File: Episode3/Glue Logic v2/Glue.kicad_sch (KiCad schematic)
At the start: 8 parts, among them U7 ATF22V10C, U8 ATF750CL, U9 ATF750CL

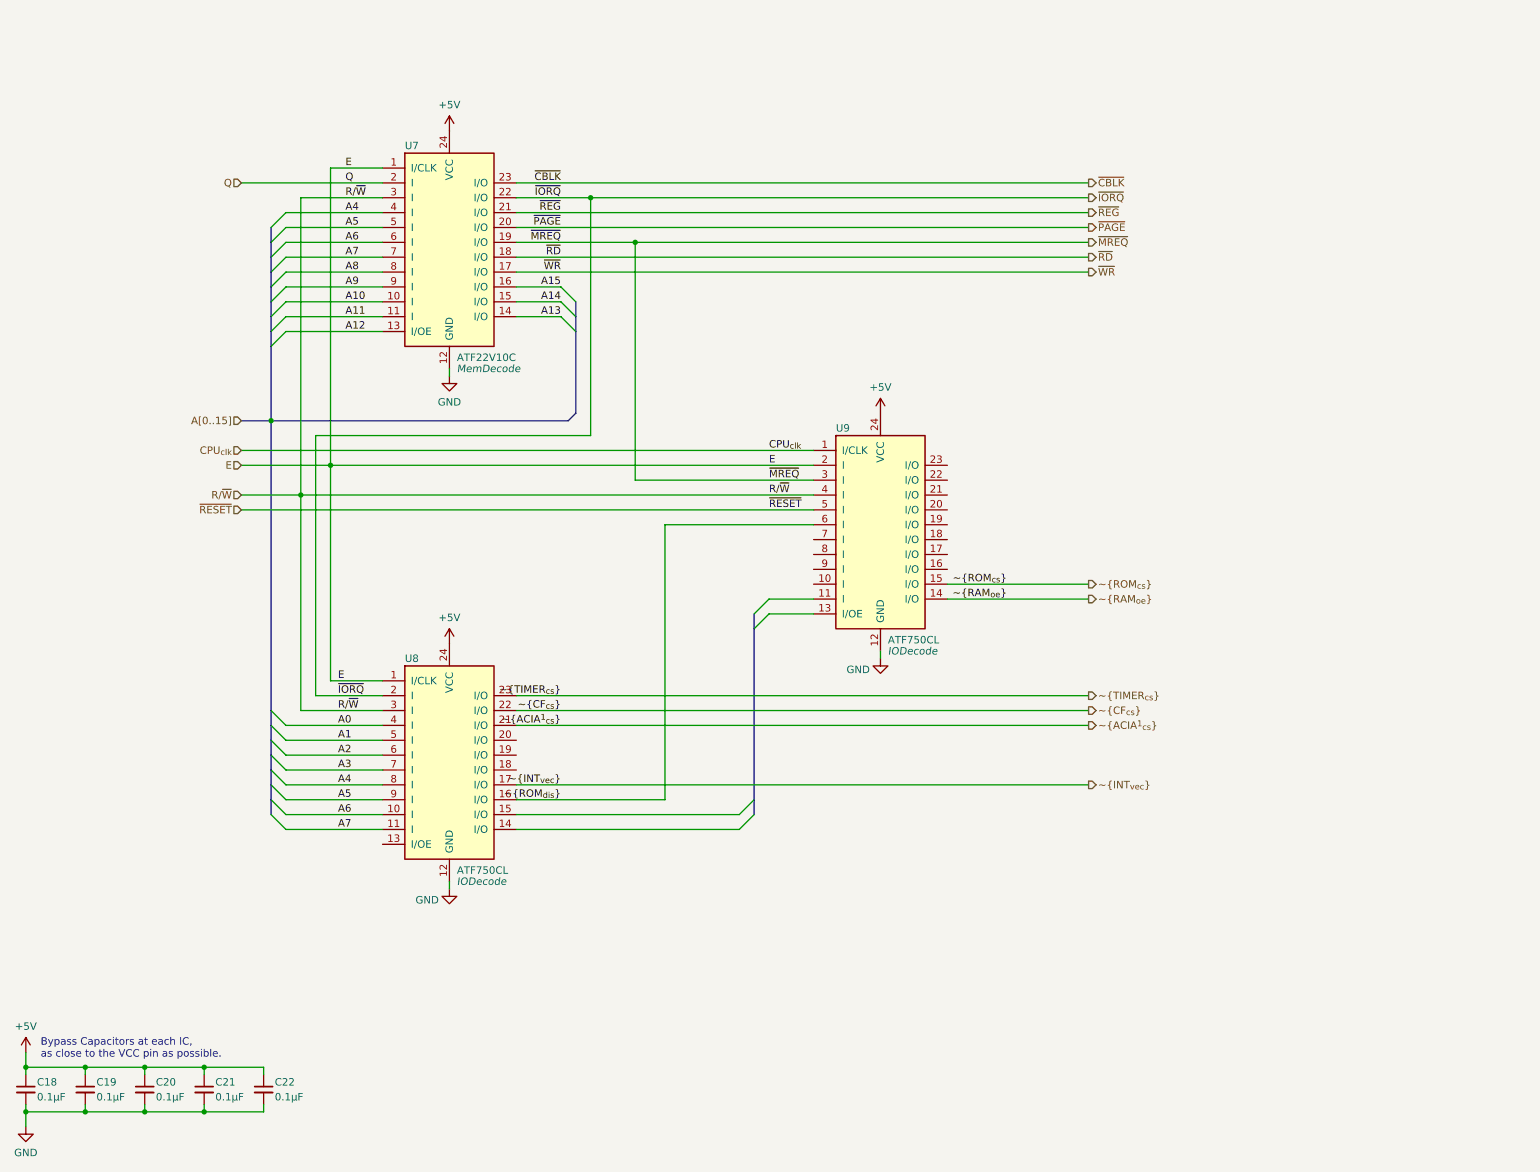
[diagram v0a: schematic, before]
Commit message: changed strategy and simplified things
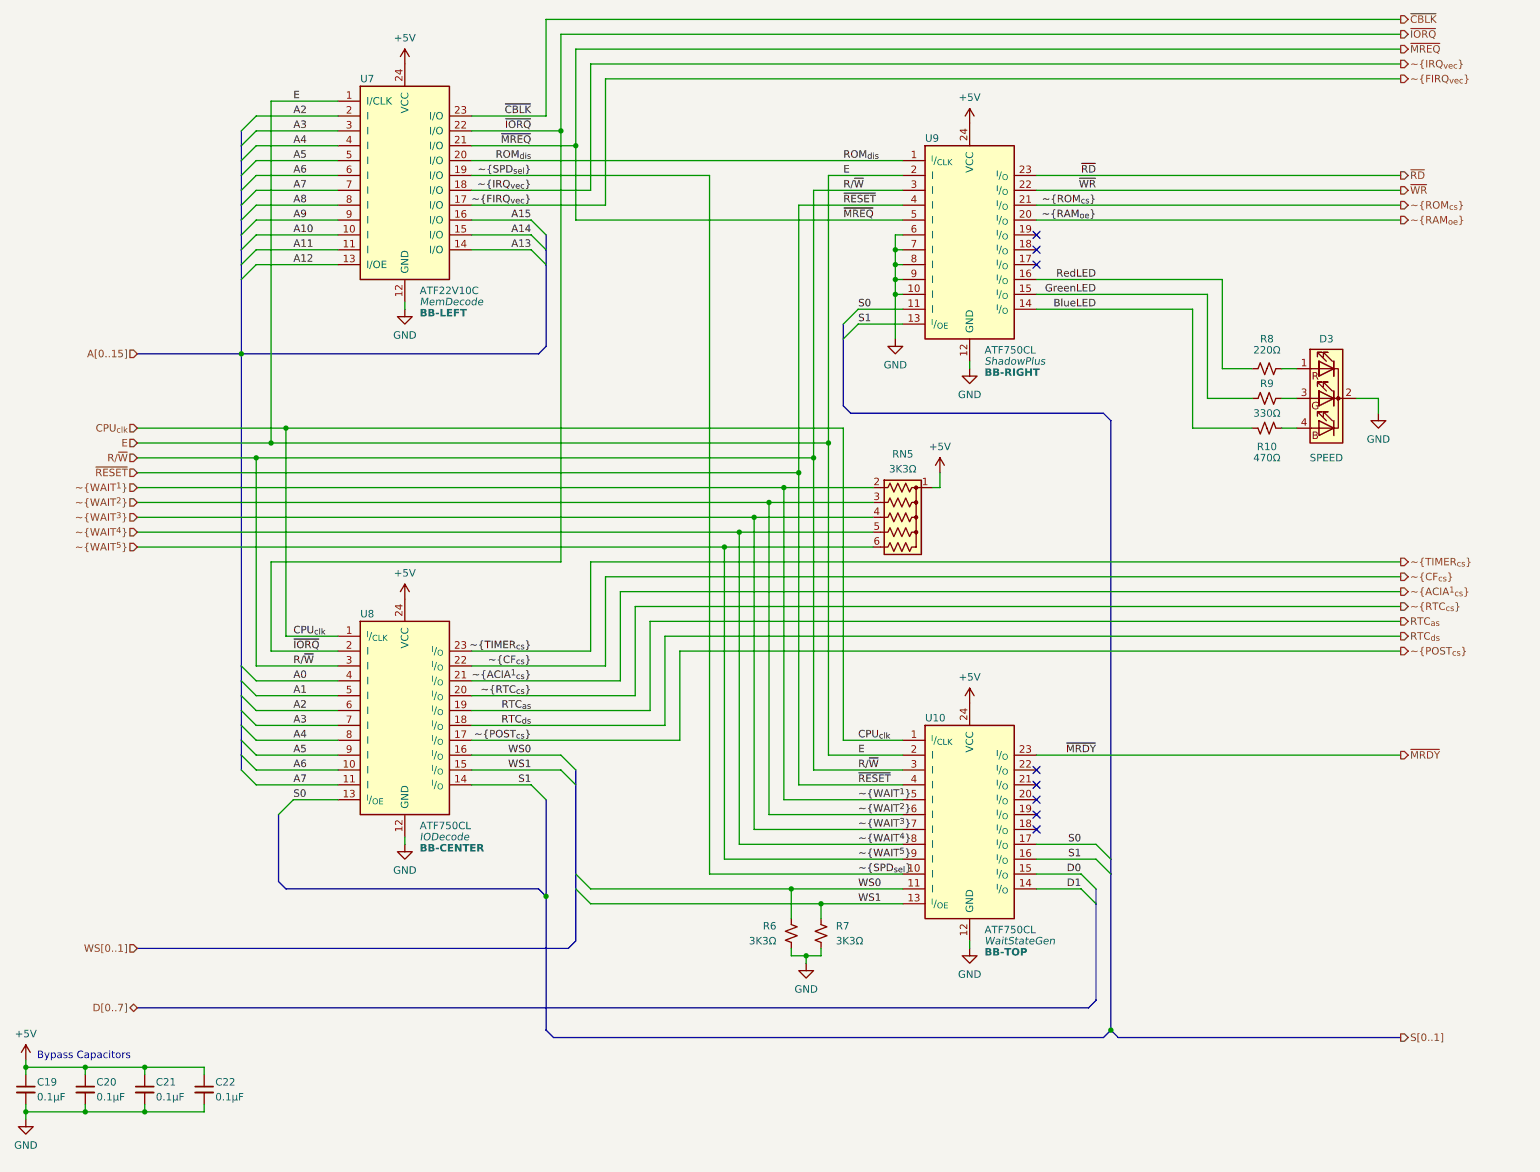
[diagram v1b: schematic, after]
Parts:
- removed C22: 0.1µF, symbol Device:C_Small
- added D3: SPEED, symbol Device:LED_RKGB
- added R10: 470Ω, symbol Device:R_Small_US
- added R6, R7: 3K3Ω, symbol Device:R_Small_US
- added R8: 220Ω, symbol Device:R_Small_US
- added R9: 330Ω, symbol Device:R_Small_US
- added RN5: 3K3Ω, Resistor_THT:R_Array_SIP6, symbol Device:R_Network05_US
- added U9: ATF750CL, Package_DIP:DIP-24_W7.62mm_Socket_LongPads, symbol MicroHobbyist:ATF750C
- U10: renamed from U9; symbol MicroHobbyist:ATF22V10C -> MicroHobbyist:ATF750C; File IODecode -> WaitStateGen; Position BB-Center -> BB-TOP
- U7: Position BB-Left -> BB-LEFT
- U8: symbol MicroHobbyist:ATF22V10C -> MicroHobbyist:ATF750C; Position BB-Center -> BB-CENTER
- renumbered C18 to C19, C19 to C20, C20 to C21, C21 to C22
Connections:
- net Q is gone; now on net A2: U7.2 (I)
- net ~{REG} is gone; now on net ~{MREQ}: U7.21 (I/O)
- net +5V: now also RN5.1 (common), U9.24 (VCC)
- net A3: now also U7.3 (I)
- net CPU_{clk}: now also U8.1 (^{I}/_{CLK})
- net E: now also U9.2 (I); no longer U8.1 (I/CLK)
- net GND: now also D3.2 (K), R6.1, R7.1, U9.10 (I), U9.12 (GND), U9.6 (I), U9.7 (I), U9.8 (I), U9.9 (I)
- net R/~{W}: now also U10.3 (I), U9.3 (I); no longer U10.4 (I), U7.3 (I)
- net ~{MREQ}: now also U9.5 (I); no longer U10.3 (I), U7.19 (I/O)
- net ~{RAM_{oe}}: now also U9.20 (^{I}/_{O}); no longer U10.14 (I/O)
- net ~{RD}: now also U9.23 (^{I}/_{O}); no longer U7.18 (I/O)
- net ~{RESET}: now also U10.4 (I), U9.4 (I); no longer U10.5 (I)
- net ~{ROM_{cs}}: now also U9.21 (^{I}/_{O}); no longer U10.15 (I/O)
- net ~{WR}: now also U9.22 (^{I}/_{O}); no longer U7.17 (I/O)
- net S0: now reaches U8.13 (^{I}/_{OE})
- net S0: now also U10.17 (^{I}/_{O}), U9.11 (I)
- net S1: now reaches U8.14 (^{I}/_{O})
- net S1: now also U10.16 (^{I}/_{O}), U9.13 (^{I}/_{OE})
- net WS1: now reaches U8.15 (^{I}/_{O})
- net WS1: now also U10.13 (^{I}/_{OE}), R7.2
- net RTC_{ds}: now reaches U8.18 (^{I}/_{O})
- net RTC_{as}: now reaches U8.19 (^{I}/_{O})
- net ~{RTC_{cs}}: now reaches U8.20 (^{I}/_{O})
- net ~{SPD_{sel}}: now reaches U10.10 (I)
- net ~{SPD_{sel}}: now also U7.19 (I/O)
- net WS0: now reaches U10.11 (I)
- net WS0: now also U8.16 (^{I}/_{O}), R6.2
- net ~{MRDY}: now reaches U10.23 (^{I}/_{O})
- net ~{WAIT^{3}}: now reaches U10.7 (I)
- net ~{WAIT^{3}}: now also RN5.4 (R3)
- net ~{WAIT^{4}}: now reaches U10.8 (I)
- net ~{WAIT^{4}}: now also RN5.5 (R4)
- net ~{WAIT^{5}}: now reaches U10.9 (I)
- net ~{WAIT^{5}}: now also RN5.6 (R5)
- net ~{INT_{vec}} renamed ~{POST_{cs}}
- net ~{PAGE} renamed ROM_{dis}
- net ROM_{dis}: now also U9.1 (^{I}/_{CLK})
- net ~{ROM_{dis}} renamed ~{WAIT^{2}}
- net ~{WAIT^{2}}: now also RN5.3 (R2); no longer U8.16 (I/O)
- new net: D3.1 (RA), R8.2
- new net: D3.3 (GA), R9.2
- new net: D3.4 (BA), R10.2
- new net BlueLED: R10.1, U9.14 (^{I}/_{O})
- new net D0: U10.15 (^{I}/_{O})
- new net D1: U10.14 (^{I}/_{O})
- new net GreenLED: R9.1, U9.15 (^{I}/_{O})
- new net RedLED: R8.1, U9.16 (^{I}/_{O})
- new net ~{FIRQ_{vec}}: U7.17 (I/O)
- new net ~{IRQ_{vec}}: U7.18 (I/O)
- new net ~{WAIT^{1}}: RN5.2 (R1), U10.5 (I)
- no-connect marks 0 -> 8
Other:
- note added: "Bypass Capacitors"
- note removed: "Bypass Capacitors at each IC, as close to the VCC pin as possible."
- moved on the sheet: U10, U7, U8

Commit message: Massive changes to the PLD code (tested) - Minor changes to the Schematic
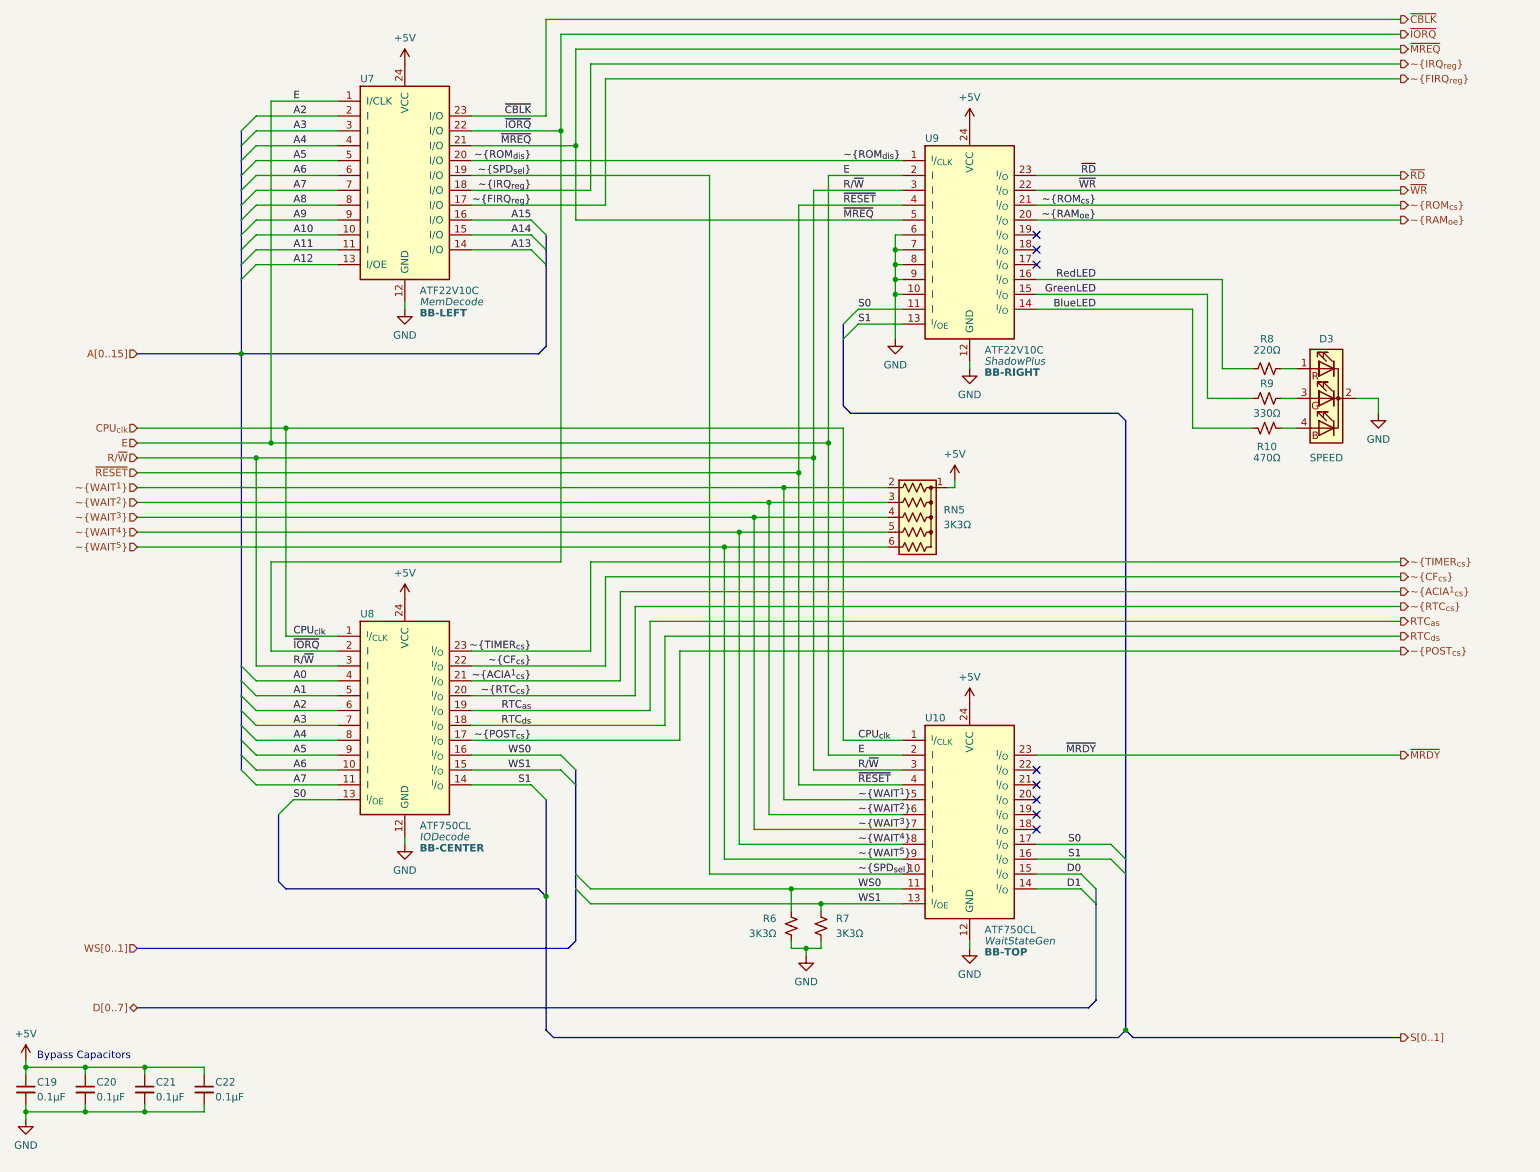
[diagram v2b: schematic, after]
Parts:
- U9: value ATF750CL -> ATF22V10C
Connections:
- net ROM_{dis} renamed ~{ROM_{dis}}
- net ~{FIRQ_{vec}} renamed ~{FIRQ_{reg}}
- net ~{IRQ_{vec}} renamed ~{IRQ_{reg}}
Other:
- title: Programmable Logic Devices -> Glue Logic with PLDs
- moved on the sheet: R6, R7, RN5
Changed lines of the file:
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@@
 	(paper "USLetter")
 	(title_block
-		(title "Programmable Logic Devices")
-		(date "2025-12-06")
+		(title "Glue Logic with PLDs")
+		(date "2026-02-07")
 		(rev "2.0")
 		(company "MicroHobbyist")
@@
 	)
 	(junction
-		(at 198.12 185.42)
+		(at 200.66 185.42)
 		(diameter 0)
 		(color 0 0 0 0)
@@
 	)
 	(junction
-		(at 146.05 172.72)
+		(at 146.05 171.45)
 		(diameter 0)
 		(color 0 0 0 0)
@@
 	)
 	(bus_entry
-		(at 195.58 156.21)
+		(at 198.12 156.21)
 		(size 2.54 2.54)
 		(stroke
@@
 	)
 	(bus_entry
-		(at 195.58 153.67)
+		(at 198.12 153.67)
 		(size 2.54 2.54)
 		(stroke
@@
 	(wire
 		(pts
-			(xy 139.7 95.25) (xy 157.48 95.25)
+			(xy 139.7 95.25) (xy 160.02 95.25)
 		)
 		(stroke
@@
 	(wire
 		(pts
-			(xy 143.51 171.45) (xy 143.51 172.72)
+			(xy 143.51 170.18) (xy 143.51 171.45)
 		)
 		(stroke
@@
 	(bus
 		(pts
-			(xy 199.39 186.69) (xy 247.65 186.69)
+			(xy 201.93 186.69) (xy 247.65 186.69)
 		)
 		(stroke
@@
 	(wire
 		(pts
-			(xy 167.64 92.71) (xy 168.91 92.71)
+			(xy 170.18 92.71) (xy 171.45 92.71)
 		)
 		(stroke
@@
 	(wire
 		(pts
-			(xy 146.05 172.72) (xy 148.59 172.72)
+			(xy 146.05 171.45) (xy 148.59 171.45)
 		)
 		(stroke
@@
 	(wire
 		(pts
-			(xy 132.08 102.87) (xy 157.48 102.87)
+			(xy 132.08 102.87) (xy 160.02 102.87)
 		)
 		(stroke
@@
 	(bus
 		(pts
-			(xy 198.12 156.21) (xy 198.12 158.75)
+			(xy 200.66 156.21) (xy 200.66 158.75)
 		)
 		(stroke
@@
 	(bus
 		(pts
-			(xy 198.12 81.28) (xy 196.85 80.01)
+			(xy 200.66 81.28) (xy 199.39 80.01)
 		)
 		(stroke
@@
 	(wire
 		(pts
-			(xy 185.42 156.21) (xy 195.58 156.21)
+			(xy 185.42 156.21) (xy 198.12 156.21)
 		)
 		(stroke
@@
 	(bus
 		(pts
-			(xy 198.12 185.42) (xy 199.39 186.69)
+			(xy 200.66 185.42) (xy 201.93 186.69)
 		)
 		(stroke
@@
 	(wire
 		(pts
-			(xy 168.91 90.17) (xy 168.91 92.71)
+			(xy 171.45 91.44) (xy 171.45 92.71)
 		)
 		(stroke
@@
 	(wire
 		(pts
-			(xy 148.59 163.83) (xy 148.59 166.37)
+			(xy 148.59 163.83) (xy 148.59 165.1)
 		)
 		(stroke
@@
 	(bus
 		(pts
-			(xy 198.12 185.42) (xy 196.85 186.69)
+			(xy 200.66 185.42) (xy 199.39 186.69)
 		)
 		(stroke
@@
 	(bus
 		(pts
-			(xy 102.87 186.69) (xy 196.85 186.69)
+			(xy 102.87 186.69) (xy 199.39 186.69)
 		)
 		(stroke
@@
 	(wire
 		(pts
-			(xy 142.24 92.71) (xy 157.48 92.71)
+			(xy 142.24 92.71) (xy 160.02 92.71)
 		)
 		(stroke
@@
 	(wire
 		(pts
-			(xy 134.62 100.33) (xy 157.48 100.33)
+			(xy 134.62 100.33) (xy 160.02 100.33)
 		)
 		(stroke
@@
 	(bus
 		(pts
-			(xy 196.85 80.01) (xy 153.67 80.01)
+			(xy 199.39 80.01) (xy 153.67 80.01)
 		)
 		(stroke
@@
 	(wire
 		(pts
-			(xy 185.42 153.67) (xy 195.58 153.67)
+			(xy 185.42 153.67) (xy 198.12 153.67)
 		)
 		(stroke
@@
 	(wire
 		(pts
-			(xy 148.59 171.45) (xy 148.59 172.72)
+			(xy 148.59 170.18) (xy 148.59 171.45)
 		)
 		(stroke
@@
 	(bus
 		(pts
-			(xy 198.12 158.75) (xy 198.12 185.42)
+			(xy 200.66 158.75) (xy 200.66 185.42)
 		)
 		(stroke
@@
 	(wire
 		(pts
-			(xy 143.51 172.72) (xy 146.05 172.72)
+			(xy 143.51 171.45) (xy 146.05 171.45)
 		)
 		(stroke
@@
 	(wire
 		(pts
-			(xy 137.16 97.79) (xy 157.48 97.79)
+			(xy 137.16 97.79) (xy 160.02 97.79)
 		)
 		(stroke
@@
 	(bus
 		(pts
-			(xy 198.12 156.21) (xy 198.12 81.28)
+			(xy 200.66 156.21) (xy 200.66 81.28)
 		)
 		(stroke
@@
 	(wire
 		(pts
-			(xy 146.05 172.72) (xy 146.05 173.99)
+			(xy 146.05 171.45) (xy 146.05 172.72)
 		)
 		(stroke
@@
 	(wire
 		(pts
-			(xy 143.51 161.29) (xy 143.51 166.37)
+			(xy 143.51 161.29) (xy 143.51 165.1)
 		)
 		(stroke
@@
 		)
 	)
-	(label "ROM_{dis}"
+	(label "~{ROM_{dis}}"
 		(at 152.4 36.83 0)
 		(effects
@@
 		)
 	)
-	(label "~{FIRQ_{vec}}"
+	(label "~{FIRQ_{reg}}"
 		(at 99.06 44.45 180)
 		(effects
@@
 		)
 	)
-	(label "ROM_{dis}"
+	(label "~{ROM_{dis}}"
 		(at 99.06 36.83 180)
 		(effects
@@
 		)
 	)
-	(label "~{IRQ_{vec}}"
+	(label "~{IRQ_{reg}}"
 		(at 99.06 41.91 180)
 		(effects
@@
 		)
 	)
-	(hierarchical_label "~{IRQ_{vec}}"
+	(hierarchical_label "~{IRQ_{reg}}"
 		(shape output)
 		(at 247.65 20.32 0)
@@
 		)
 	)
-	(hierarchical_label "~{FIRQ_{vec}}"
+	(hierarchical_label "~{FIRQ_{reg}}"
 		(shape output)
 		(at 247.65 22.86 0)
@@
 	(symbol
 		(lib_id "power:+5V")
-		(at 168.91 90.17 0)
+		(at 171.45 91.44 0)
 		(unit 1)
 		(exclude_from_sim no)
@@
 		(dnp no)
 		(property "Reference" "#PWR042"
-			(at 168.91 93.98 0)
+			(at 171.45 95.25 0)
 			(effects
 				(font
@@
 		)
 		(property "Value" "+5V"
-			(at 168.91 85.725 0)
+			(at 171.45 86.995 0)
 			(effects
 				(font
@@
 		)
 		(property "Footprint" ""
-			(at 168.91 90.17 0)
+			(at 171.45 91.44 0)
 			(effects
 				(font
@@
 		)
 		(property "Datasheet" ""
-			(at 168.91 90.17 0)
+			(at 171.45 91.44 0)
 			(effects
 				(font
@@
 		)
 		(property "Description" "Power symbol creates a global label with name \"+5V\""
-			(at 168.91 90.17 0)
+			(at 171.45 91.44 0)
 			(effects
 				(font
@@
 	(symbol
 		(lib_id "Device:R_Network05_US")
-		(at 162.56 97.79 270)
+		(at 165.1 97.79 270)
 		(unit 1)
 		(exclude_from_sim no)
@@
 		(dnp no)
 		(property "Reference" "RN5"
-			(at 162.56 86.995 90)
+			(at 169.545 96.52 90)
 			(effects
 				(font
 					(size 1.27 1.27)
 				)
+				(justify left)
 			)
 		)
 		(property "Value" "3K3Ω"
-			(at 162.56 89.535 90)
+			(at 169.545 99.06 90)
 			(effects
 				(font
 					(size 1.27 1.27)
 				)
+				(justify left)
 			)
 		)
 		(property "Footprint" "Resistor_THT:R_Array_SIP6"
-			(at 162.56 107.315 90)
+			(at 165.1 107.315 90)
 			(effects
 				(font
@@
 		)
 		(property "Datasheet" "http://www.vishay.com/docs/31509/csc.pdf"
-			(at 162.56 97.79 0)
+			(at 165.1 97.79 0)
 			(effects
 				(font
@@
 		)
 		(property "Description" "5 resistor network, star topology, bussed resistors, small US symbol"
-			(at 162.56 97.79 0)
+			(at 165.1 97.79 0)
 			(effects
 				(font
@@
 		(lib_name "GND_1")
 		(lib_id "power:GND")
-		(at 146.05 173.99 0)
+		(at 146.05 172.72 0)
 		(unit 1)
 		(exclude_from_sim no)
@@
 		(dnp no)
 		(property "Reference" "#PWR040"
-			(at 146.05 180.34 0)
+			(at 146.05 179.07 0)
 			(effects
 				(font
@@
 		)
 		(property "Value" "GND"
-			(at 146.05 178.435 0)
+			(at 146.05 177.165 0)
 			(effects
 				(font
@@
 		)
 		(property "Footprint" ""
-			(at 146.05 173.99 0)
+			(at 146.05 172.72 0)
 			(effects
 				(font
@@
 		)
 		(property "Datasheet" ""
-			(at 146.05 173.99 0)
+			(at 146.05 172.72 0)
 			(effects
 				(font
@@
 		)
 		(property "Description" "Power symbol creates a global label with name \"GND\" , ground"
-			(at 146.05 173.99 0)
+			(at 146.05 172.72 0)
 			(effects
 				(font
@@
 	(symbol
 		(lib_id "Device:R_Small_US")
-		(at 148.59 168.91 180)
+		(at 148.59 167.64 180)
 		(unit 1)
 		(exclude_from_sim no)
@@
 		(fields_autoplaced yes)
 		(property "Reference" "R7"
-			(at 151.13 167.6399 0)
+			(at 151.13 166.3699 0)
 			(effects
 				(font
@@
 		)
 		(property "Value" "3K3Ω"
-			(at 151.13 170.1799 0)
+			(at 151.13 168.9099 0)
 			(effects
 				(font
@@
 		)
 		(property "Footprint" ""
-			(at 148.59 168.91 0)
+			(at 148.59 167.64 0)
 			(effects
 				(font
@@
 		)
 		(property "Datasheet" "~"
-			(at 148.59 168.91 0)
+			(at 148.59 167.64 0)
 			(effects
 				(font
@@
 		)
 		(property "Description" "Resistor, small US symbol"
-			(at 148.59 168.91 0)
+			(at 148.59 167.64 0)
 			(effects
 				(font
@@
 			)
 		)
-		(property "Value" "ATF750CL"
+		(property "Value" "ATF22V10C"
 			(at 176.53 69.215 0)
 			(do_not_autoplace yes)
@@
 	(symbol
 		(lib_id "Device:R_Small_US")
-		(at 143.51 168.91 180)
+		(at 143.51 167.64 180)
 		(unit 1)
 		(exclude_from_sim no)
@@
 		(dnp no)
 		(property "Reference" "R6"
-			(at 140.97 167.64 0)
+			(at 140.97 166.37 0)
 			(effects
 				(font
@@
 		)
 		(property "Value" "3K3Ω"
-			(at 140.97 170.18 0)
+			(at 140.97 168.91 0)
 			(effects
 				(font
@@
 		)
 		(property "Footprint" ""
-			(at 143.51 168.91 0)
+			(at 143.51 167.64 0)
 			(effects
 				(font
@@
 		)
 		(property "Datasheet" "~"
-			(at 143.51 168.91 0)
+			(at 143.51 167.64 0)
 			(effects
 				(font
@@
 		)
 		(property "Description" "Resistor, small US symbol"
-			(at 143.51 168.91 0)
+			(at 143.51 167.64 0)
 			(effects
 				(font
